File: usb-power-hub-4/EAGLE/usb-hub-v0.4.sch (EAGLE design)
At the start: 37 parts, among them U1 RICHTEKRT9715AGBR, U2 RICHTEKRT9715AGBR, U3 RICHTEKRT9715AGBR, U4 RICHTEKRT9715AGBR

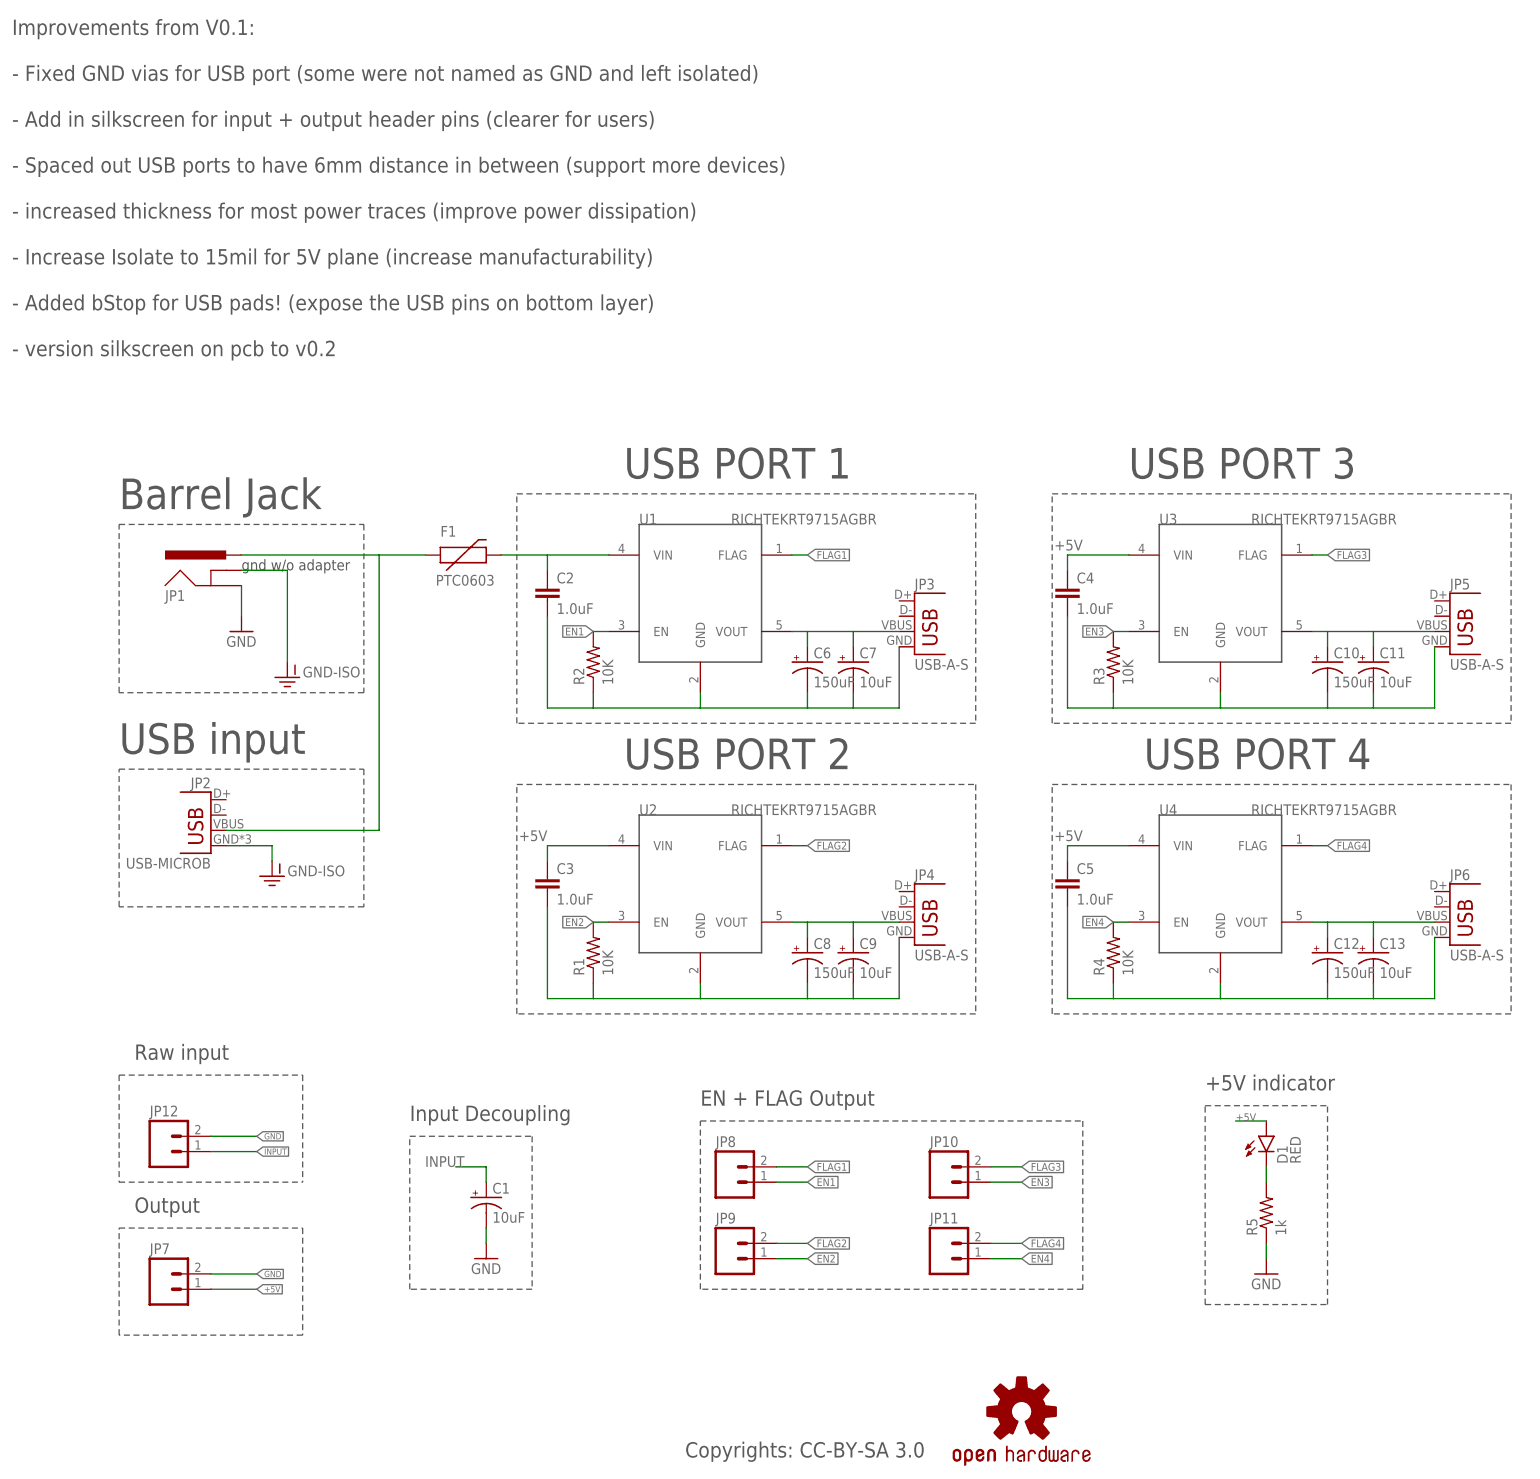
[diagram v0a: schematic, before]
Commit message: V0.4 update!
- Improved DFM for R1 to R4

- Improved silkscreen text size and readibility
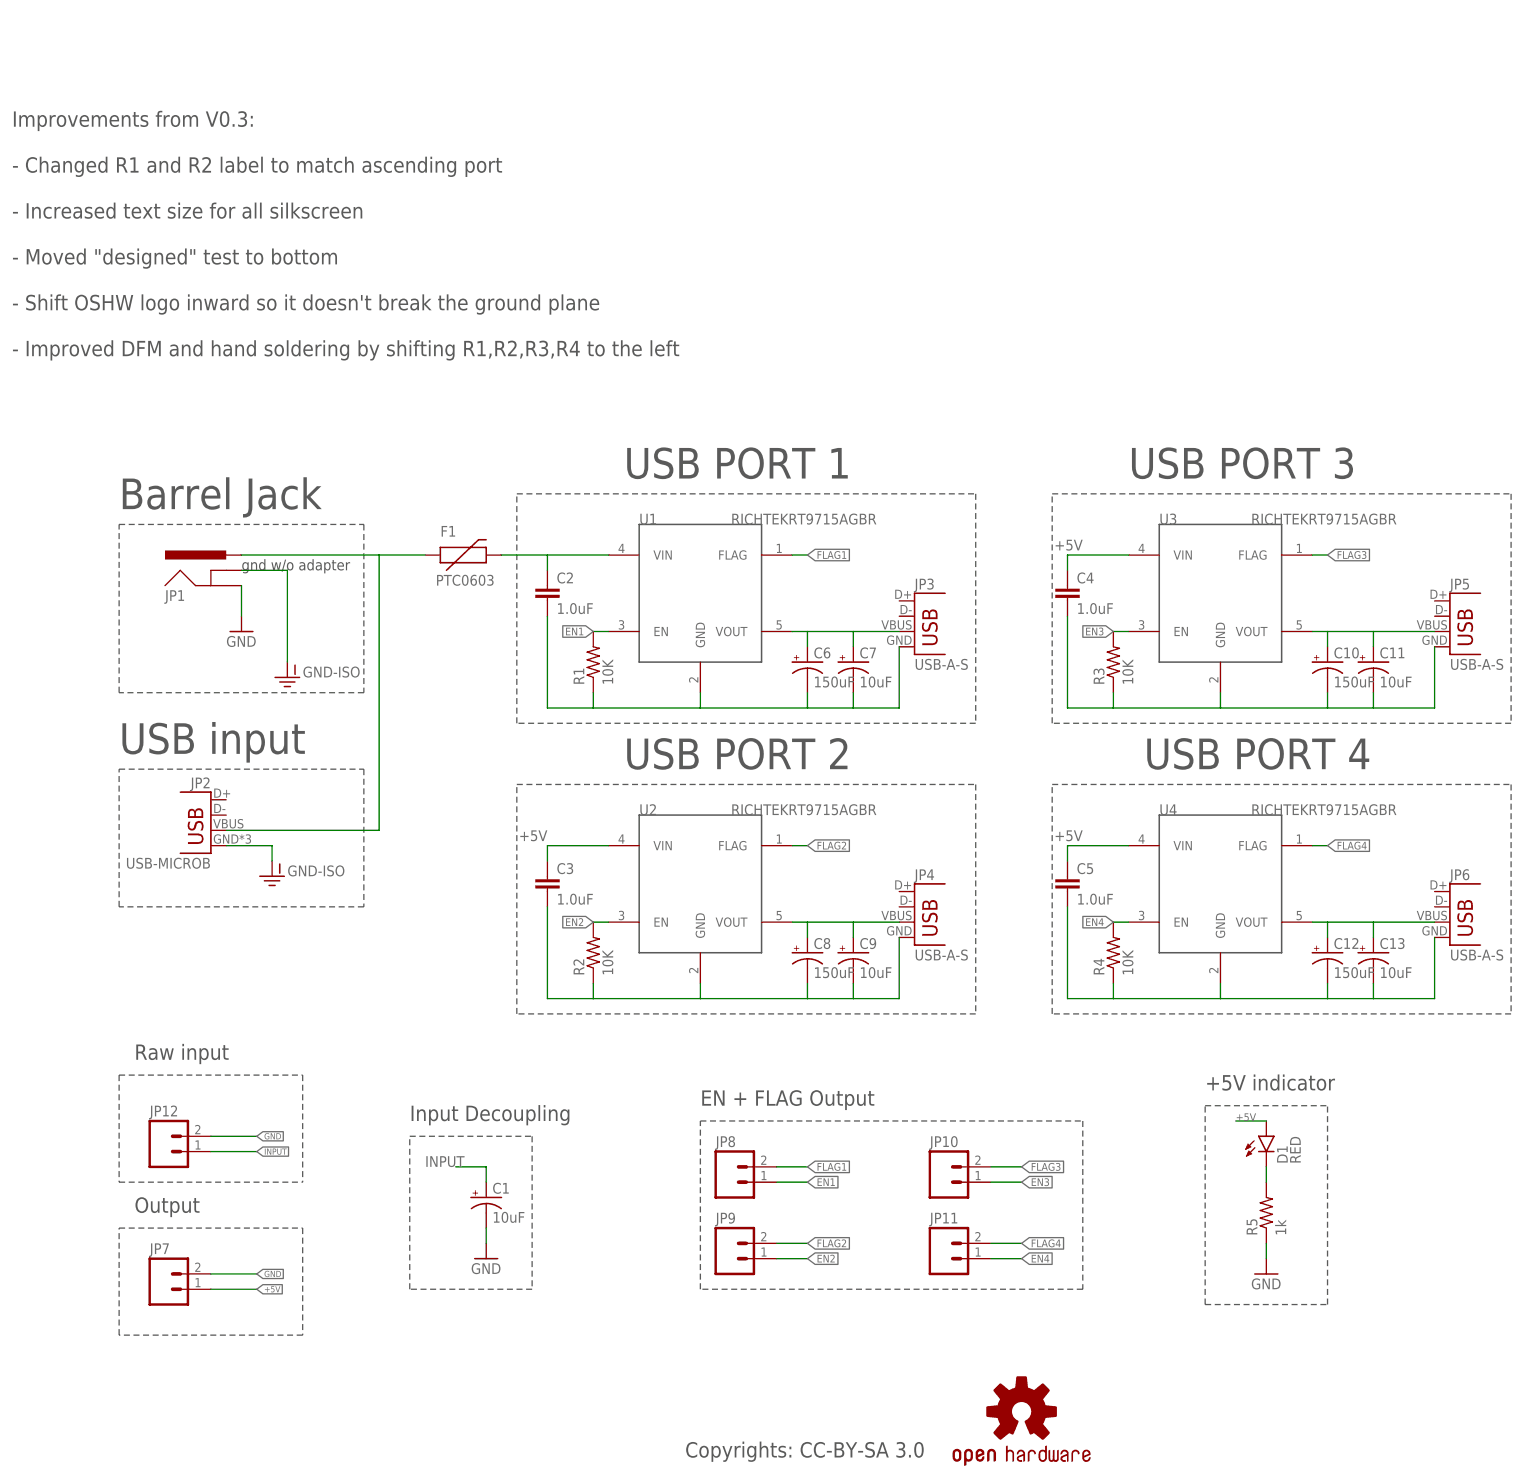
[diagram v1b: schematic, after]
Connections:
- net EN1: now also R1.2; no longer R2.2
- net EN2: now also R2.2; no longer R1.2
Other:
- note added: "Improvements from V0.3: - Changed R1 and R2 label to match ascending port - Increased text size for all silkscreen - Moved "designed" test to bottom - Shift OSHW logo inward so it doesn't break the ground plane - Improved DFM and hand soldering by shifting R1,R2,R3,R4 to the left"
- note removed: "Improvements from V0.1: - Fixed GND vias for USB port (some were not named as GND and left isolated) - Add in silkscreen for input + output header pins (clearer for users) - Spaced out USB ports to have 6mm distance in between (support more devices) - increased thickness for most power traces (improve power dissipation) - Increase Isolate to 15mil for 5V plane (increase manufacturability) - Added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"
- moved on the sheet: R1, R2
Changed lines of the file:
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@@
 <attributes>
 <attribute name="CNAME" value="USB Power hub x4"/>
-<attribute name="CREVISION" value="V0.2.1"/>
+<attribute name="CREVISION" value="V0.4"/>
 <attribute name="DESIGNER" value="kennethlimcp"/>
 </attributes>
@@
 <part name="JP2" library="SparkFun-Connectors" deviceset="USB" device="-MICROB"/>
 <part name="GND-ISO2" library="SparkFun-Aesthetics" deviceset="GND-ISO" device=""/>
-<part name="R2" library="SparkFun-Resistors" deviceset="RESISTOR" device="0402" value="10K"/>
+<part name="R1" library="SparkFun-Resistors" deviceset="RESISTOR" device="0402" value="10K"/>
 <part name="C6" library="SparkFun-Capacitors" deviceset="CAP_POL" device="D" value="150uF"/>
 <part name="C7" library="SparkFun-Capacitors" deviceset="10UF-16V-10%(TANT)" device="" value="10uF"/>
@@
 <part name="C12" library="SparkFun-Capacitors" deviceset="CAP_POL" device="D" value="150uF"/>
 <part name="C13" library="SparkFun-Capacitors" deviceset="10UF-16V-10%(TANT)" device="" value="10uF"/>
-<part name="R1" library="SparkFun-Resistors" deviceset="RESISTOR" device="0402" value="10K"/>
+<part name="R2" library="SparkFun-Resistors" deviceset="RESISTOR" device="0402" value="10K"/>
 <part name="R3" library="SparkFun-Resistors" deviceset="RESISTOR" device="0402" value="10K"/>
 <part name="R4" library="SparkFun-Resistors" deviceset="RESISTOR" device="0402" value="10K"/>
@@
 <wire x1="195.58" y1="30.48" x2="195.58" y2="63.5" width="0.1524" layer="97" style="shortdash"/>
 <text x="195.58" y="66.04" size="2.54" layer="97" font="vector">+5V indicator</text>
-<text x="-2.54" y="187.96" size="2.54" layer="97">Improvements from V0.1:
-- Fixed GND vias for USB port (some were not named as GND and left isolated)
-- Add in silkscreen for input + output header pins (clearer for users)
-- Spaced out USB ports to have 6mm distance in between (support more devices)
-- increased thickness for most power traces (improve power dissipation)
-- Increase Isolate to 15mil for 5V plane (increase manufacturability)
-- Added bStop for USB pads! (expose the USB pins on bottom layer)
-- version silkscreen on pcb to v0.2</text>
+<text x="-2.54" y="187.96" size="2.54" layer="97">Improvements from V0.3:
+- Changed R1 and R2 label to match ascending port
+- Increased text size for all silkscreen
+- Moved "designed" test to bottom
+- Shift OSHW logo inward so it doesn't break the ground plane
+- Improved DFM and hand soldering by shifting R1,R2,R3,R4 to the left </text>
 </plain>
 <instances>
@@
 <instance part="JP2" gate="G$1" x="30.48" y="106.68" rot="MR0"/>
 <instance part="GND-ISO2" gate="G$1" x="40.64" y="101.6"/>
-<instance part="R2" gate="G$1" x="93.98" y="137.16" rot="R90"/>
+<instance part="R1" gate="G$1" x="93.98" y="137.16" rot="R90"/>
 <instance part="C6" gate="G$1" x="129.54" y="137.16"/>
 <instance part="C7" gate="G$1" x="137.16" y="137.16"/>
@@
 <instance part="C12" gate="G$1" x="215.9" y="88.9"/>
 <instance part="C13" gate="G$1" x="223.52" y="88.9"/>
-<instance part="R1" gate="G$1" x="93.98" y="88.9" rot="R90"/>
+<instance part="R2" gate="G$1" x="93.98" y="88.9" rot="R90"/>
 <instance part="R3" gate="G$1" x="180.34" y="137.16" rot="R90"/>
 <instance part="R4" gate="G$1" x="180.34" y="88.9" rot="R90"/>
@@
 <wire x1="137.16" y1="129.54" x2="129.54" y2="129.54" width="0.1524" layer="91"/>
 <wire x1="137.16" y1="132.08" x2="137.16" y2="129.54" width="0.1524" layer="91"/>
-<pinref part="R2" gate="G$1" pin="1"/>
+<pinref part="R1" gate="G$1" pin="1"/>
 <wire x1="93.98" y1="132.08" x2="93.98" y2="129.54" width="0.1524" layer="91"/>
 </segment>
@@
 <pinref part="C8" gate="G$1" pin="-"/>
 <wire x1="129.54" y1="83.82" x2="129.54" y2="81.28" width="0.1524" layer="91"/>
-<pinref part="R1" gate="G$1" pin="1"/>
+<pinref part="R2" gate="G$1" pin="1"/>
 <wire x1="93.98" y1="83.82" x2="93.98" y2="81.28" width="0.1524" layer="91"/>
 </segment>
@@
 <segment>
 <pinref part="U1" gate="G$1" pin="EN"/>
-<pinref part="R2" gate="G$1" pin="2"/>
+<pinref part="R1" gate="G$1" pin="2"/>
 <wire x1="96.52" y1="142.24" x2="93.98" y2="142.24" width="0.1524" layer="91"/>
 <label x="93.98" y="142.24" size="1.27" layer="95" rot="R180" xref="yes"/>
@@
 <segment>
 <pinref part="U2" gate="G$1" pin="EN"/>
-<pinref part="R1" gate="G$1" pin="2"/>
+<pinref part="R2" gate="G$1" pin="2"/>
 <wire x1="96.52" y1="93.98" x2="93.98" y2="93.98" width="0.1524" layer="91"/>
 <label x="93.98" y="93.98" size="1.27" layer="95" rot="R180" xref="yes"/>
